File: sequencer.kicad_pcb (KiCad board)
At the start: 4 copper layers, 120 x 60 mm, 81 parts, among them J1 AudioJack2_SwitchT, J2 AudioJack2_SwitchT, J3 AudioJack2_SwitchT, J4 Conn_ARM_JTAG_SWD_10, J5 Conn_01x06_Male, J6 Conn_01x02_Male, SW1 OS102011MS2QN1, SW10 EG1206A, SW2 OS102011MS2QN1, SW3 OS102011MS2QN1, SW4 OS102011MS2QN1, SW5 OS102011MS2QN1, SW6 OS102011MS2QN1, SW7 OS102011MS2QN1, SW8 OS102011MS2QN1, SW9 OS102011MS2QN1, U1 LM358, U2 74HC4051, U3 STM32F031K6Tx, U4 74HCT14, U5 L78L05_SOT89, U6 L78L33_SOT89, X1 ASV-8.000MHz

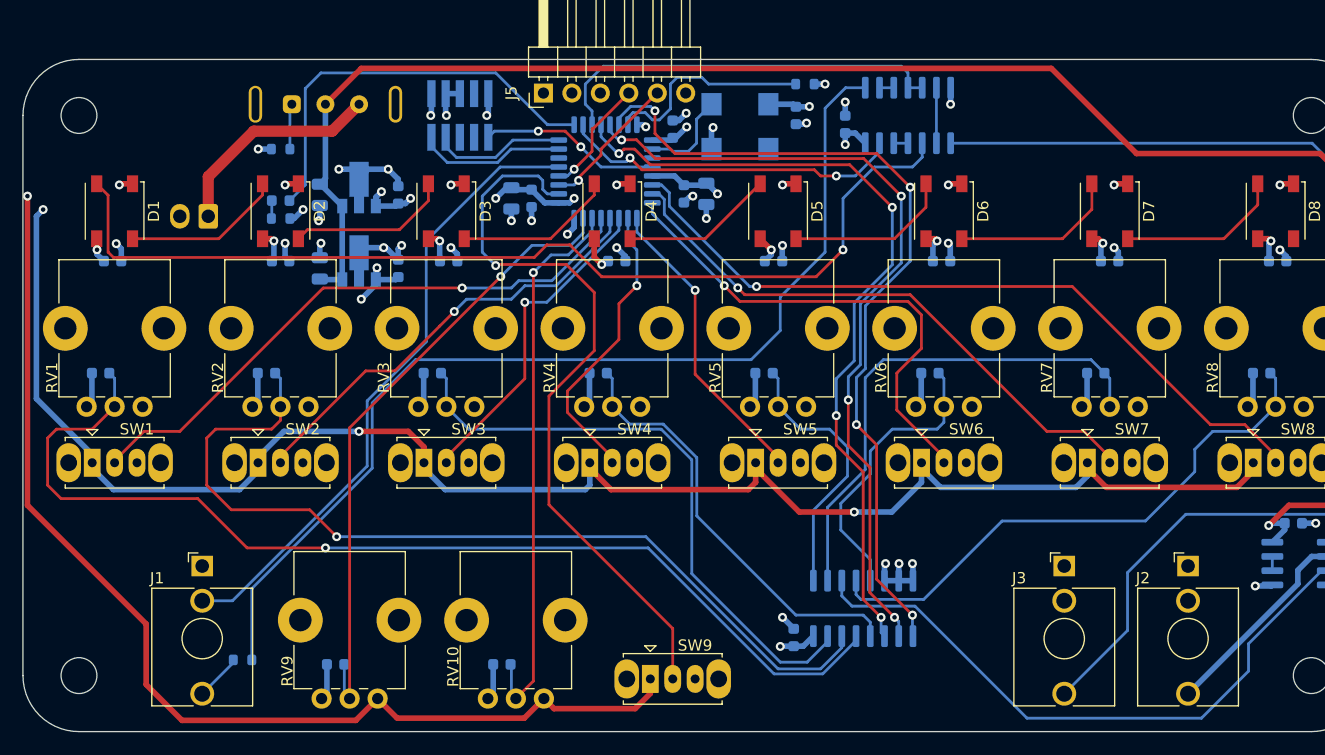
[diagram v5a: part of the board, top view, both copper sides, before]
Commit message: add labels
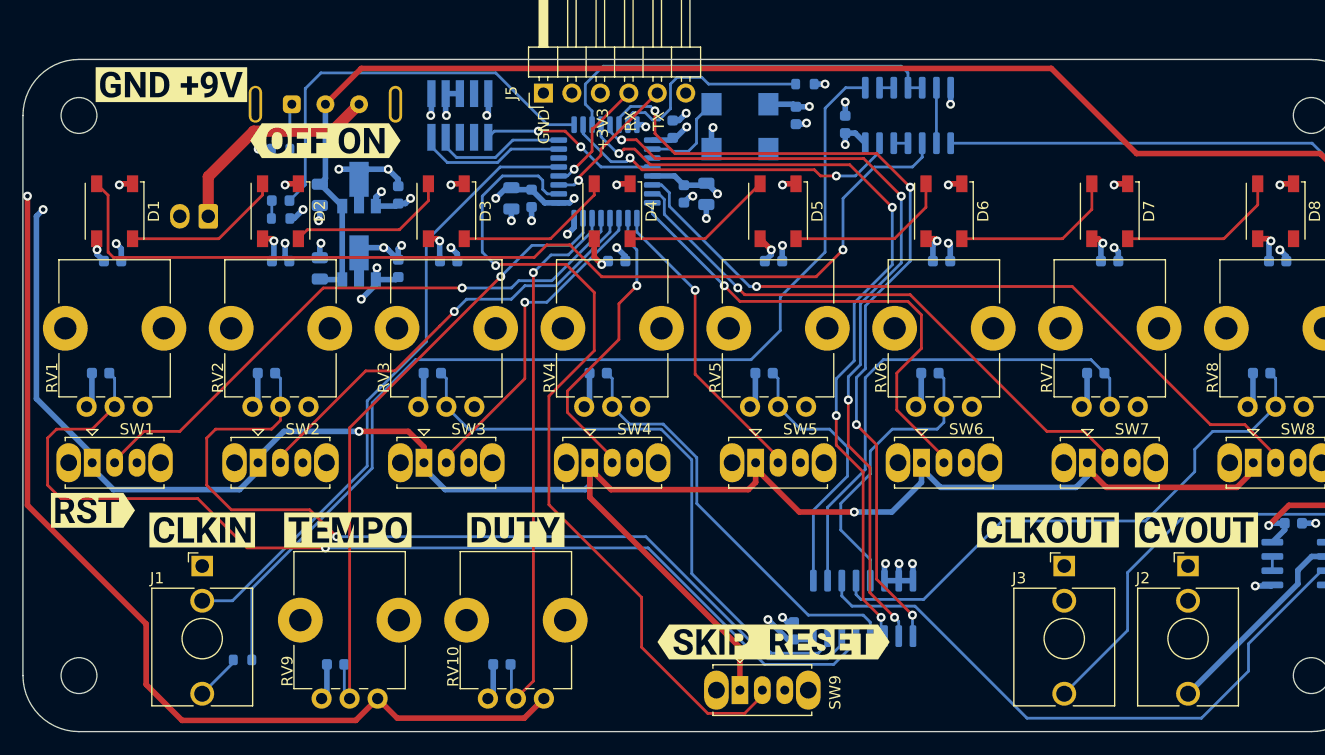
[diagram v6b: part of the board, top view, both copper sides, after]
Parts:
- added kibuzzard-63F425C8: G***, kibuzzard-63F425C8, F.Cu at (184.8, 107.0)
- added kibuzzard-63F425D0: G***, kibuzzard-63F425D0, F.Cu at (171.5, 107.0)
- added kibuzzard-63F42616: G***, kibuzzard-63F42616, F.Cu at (109.0, 107.0)
- added kibuzzard-63F42620: G***, kibuzzard-63F42620, F.Cu at (124.0, 107.0)
- added kibuzzard-63F42641: G***, kibuzzard-63F42641, F.Cu at (96.0, 107.0)
- added kibuzzard-63F42779: G***, kibuzzard-63F42779, F.Cu at (86.2, 105.2)
- added kibuzzard-63F427E2: G***, kibuzzard-63F427E2, F.Cu at (93.2, 67.2)
- added kibuzzard-63F428B8: G***, kibuzzard-63F428B8, F.Cu at (147.0, 117.0)
- added kibuzzard-63F428D5: G***, kibuzzard-63F428D5, F.Cu at (107.0, 72.2)
- moved SW9 8.06 mm to (144.0, 121.3)
- moved C17 0.60 mm to (148.8, 116.0)
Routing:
- net +3.3V: track 279.5 -> 293.6 mm
- net /skip_reset_switch: track 66.0 -> 76.4 mm
- net +5V: track 35.0 -> 36.6 mm
- net /cv_pot_2: track 81.2 -> 80.2 mm
- net /cv_pot_4: track 38.5 -> 37.8 mm
- net /cv_pot_1: track 95.3 -> 94.7 mm
- net /cv_pot_3: track 53.9 -> 53.3 mm
